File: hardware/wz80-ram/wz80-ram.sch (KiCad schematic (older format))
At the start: 4 parts, among them J1 CONN_01X32, U1 HM62256BLP-7, U2 74LS32, U3 74HC04

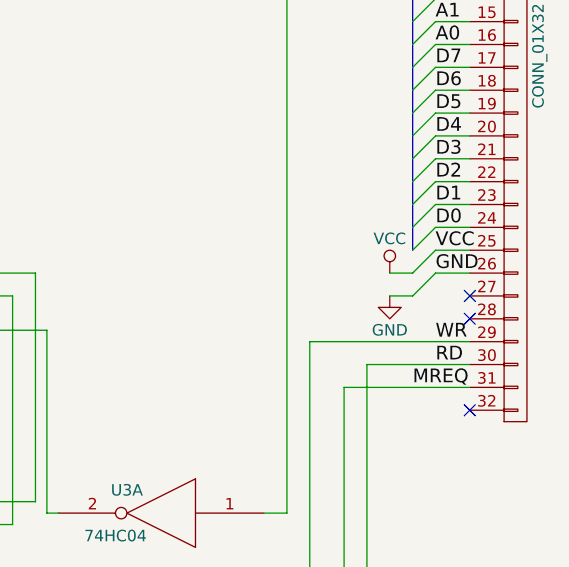
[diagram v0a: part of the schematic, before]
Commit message: Moved schematics into hardware/. Added start of software.
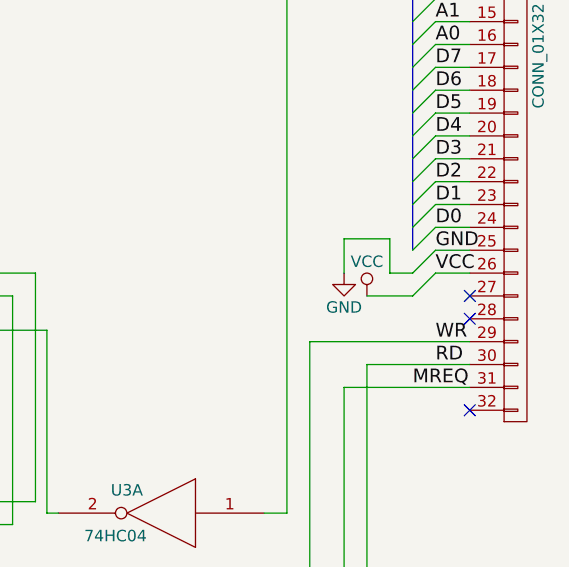
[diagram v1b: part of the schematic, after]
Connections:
- net GND: now also J1.25 (P25); no longer J1.26 (P26)
- net VCC: now also J1.26 (P26); no longer J1.25 (P25)
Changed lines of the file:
@@
 	8350 3750 8450 3650
-Wire Wire Line
-	8250 3850 8350 3850
 Wire Wire Line
 	8350 3850 8450 3750
@@
 L VCC #PWR01
 U 1 1 58D030D2
-P 8250 3750
-F 0 "#PWR01" H 8250 3600 50  0001 C CNN
-F 1 "VCC" H 8250 3900 50  0000 C CNN
-F 2 "" H 8250 3750 50  0001 C CNN
-F 3 "" H 8250 3750 50  0001 C CNN
-	1    8250 3750
+P 8150 3850
+F 0 "#PWR01" H 8150 3700 50  0001 C CNN
+F 1 "VCC" H 8150 4000 50  0000 C CNN
+F 2 "" H 8150 3850 50  0001 C CNN
+F 3 "" H 8150 3850 50  0001 C CNN
+	1    8150 3850
 	1    0    0    -1
 $EndComp
@@
 L GND #PWR02
 U 1 1 58D030F0
-P 8250 3850
-F 0 "#PWR02" H 8250 3600 50  0001 C CNN
-F 1 "GND" H 8250 3700 50  0000 C CNN
-F 2 "" H 8250 3850 50  0001 C CNN
-F 3 "" H 8250 3850 50  0001 C CNN
-	1    8250 3850
+P 8050 3750
+F 0 "#PWR02" H 8050 3500 50  0001 C CNN
+F 1 "GND" H 8050 3600 50  0000 C CNN
+F 2 "" H 8050 3750 50  0001 C CNN
+F 3 "" H 8050 3750 50  0001 C CNN
+	1    8050 3750
 	1    0    0    -1
 $EndComp
-Wire Wire Line
-	8250 3750 8350 3750
 NoConn ~ 8600 4350
 Text Label 8450 3650 0    60   ~ 0
+GND
+Text Label 8450 3750 0    60   ~ 0
 VCC
-Text Label 8450 3750 0    60   ~ 0
-GND
 Text Label 8450 4050 0    60   ~ 0
 WR
@@
 Text Label 8350 4250 0    60   ~ 0
 MREQ
+Wire Wire Line
+	8350 3850 8150 3850
+Wire Wire Line
+	8350 3750 8250 3750
+Wire Wire Line
+	8250 3750 8250 3600
+Wire Wire Line
+	8250 3600 8050 3600
+Wire Wire Line
+	8050 3600 8050 3750
 $EndSCHEMATC
